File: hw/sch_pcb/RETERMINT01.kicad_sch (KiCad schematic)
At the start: 82 parts, among them J1 Conn_02x05_Odd_Even, J10 Raspberry_Pi_4, J11 RJ45_LED_Shielded, J2 Barrel_Jack_Switch, J3 HEADER_2x05_PARALLEL, J4 HEADER_2x01_PARALLEL, J5 HEADER_2x01_PARALLEL, J6 HEADER_2x01_PARALLEL, J7 HEADER_2x01_PARALLEL, J8 u.fl, J9 HEADER_2x01_PARALLEL, M1 HOLE, M2 HOLE, M3 HOLE, M4 HOLE, Q1 BC817-25, Q2 BC817-25, U1 TPSM33606S5QRDNRQ1, U2 USBLC6-2SC6, U3 MIC5504-3.3YM5, U4 NEO-M9N, U5 ADM2483xRW, U6 ADM2483xRW, U7 ADM2483xRW

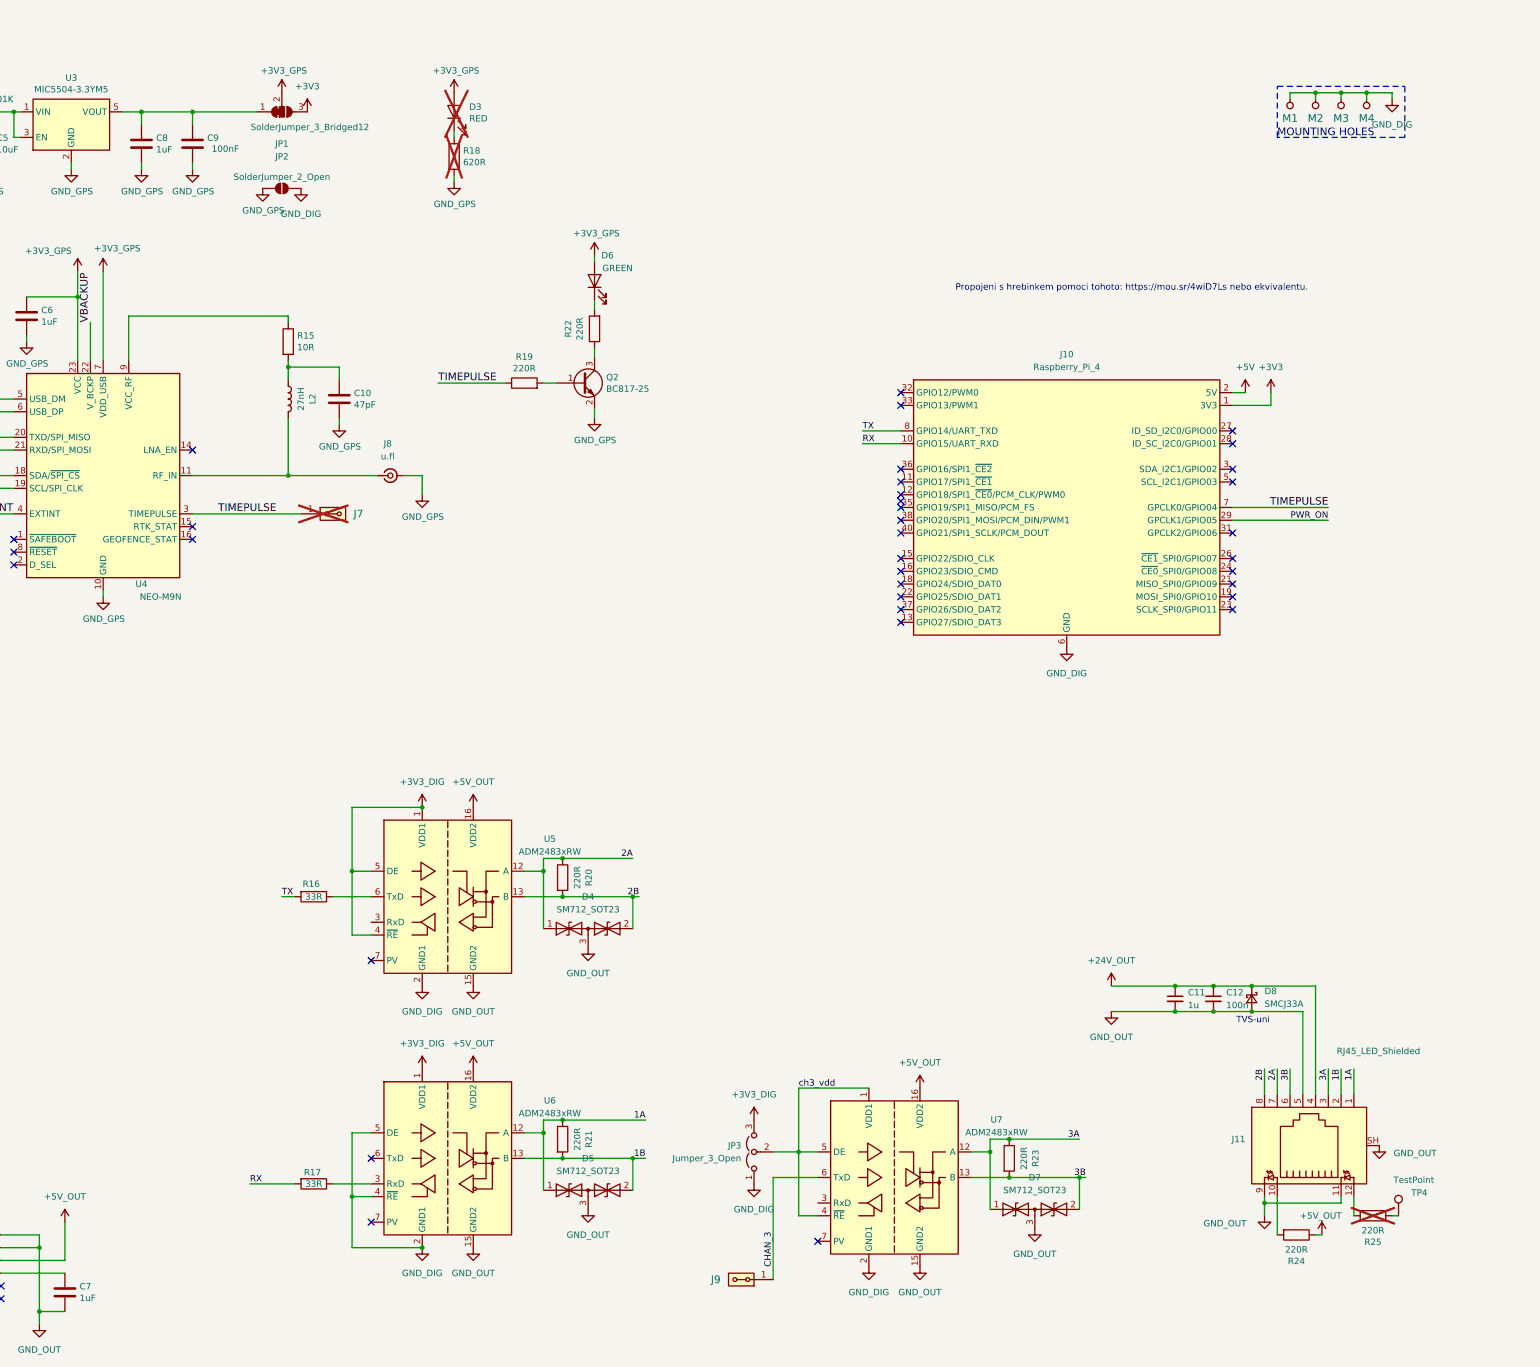
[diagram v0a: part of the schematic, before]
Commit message: Fix #2 Fix DRC errors. Improve layout.
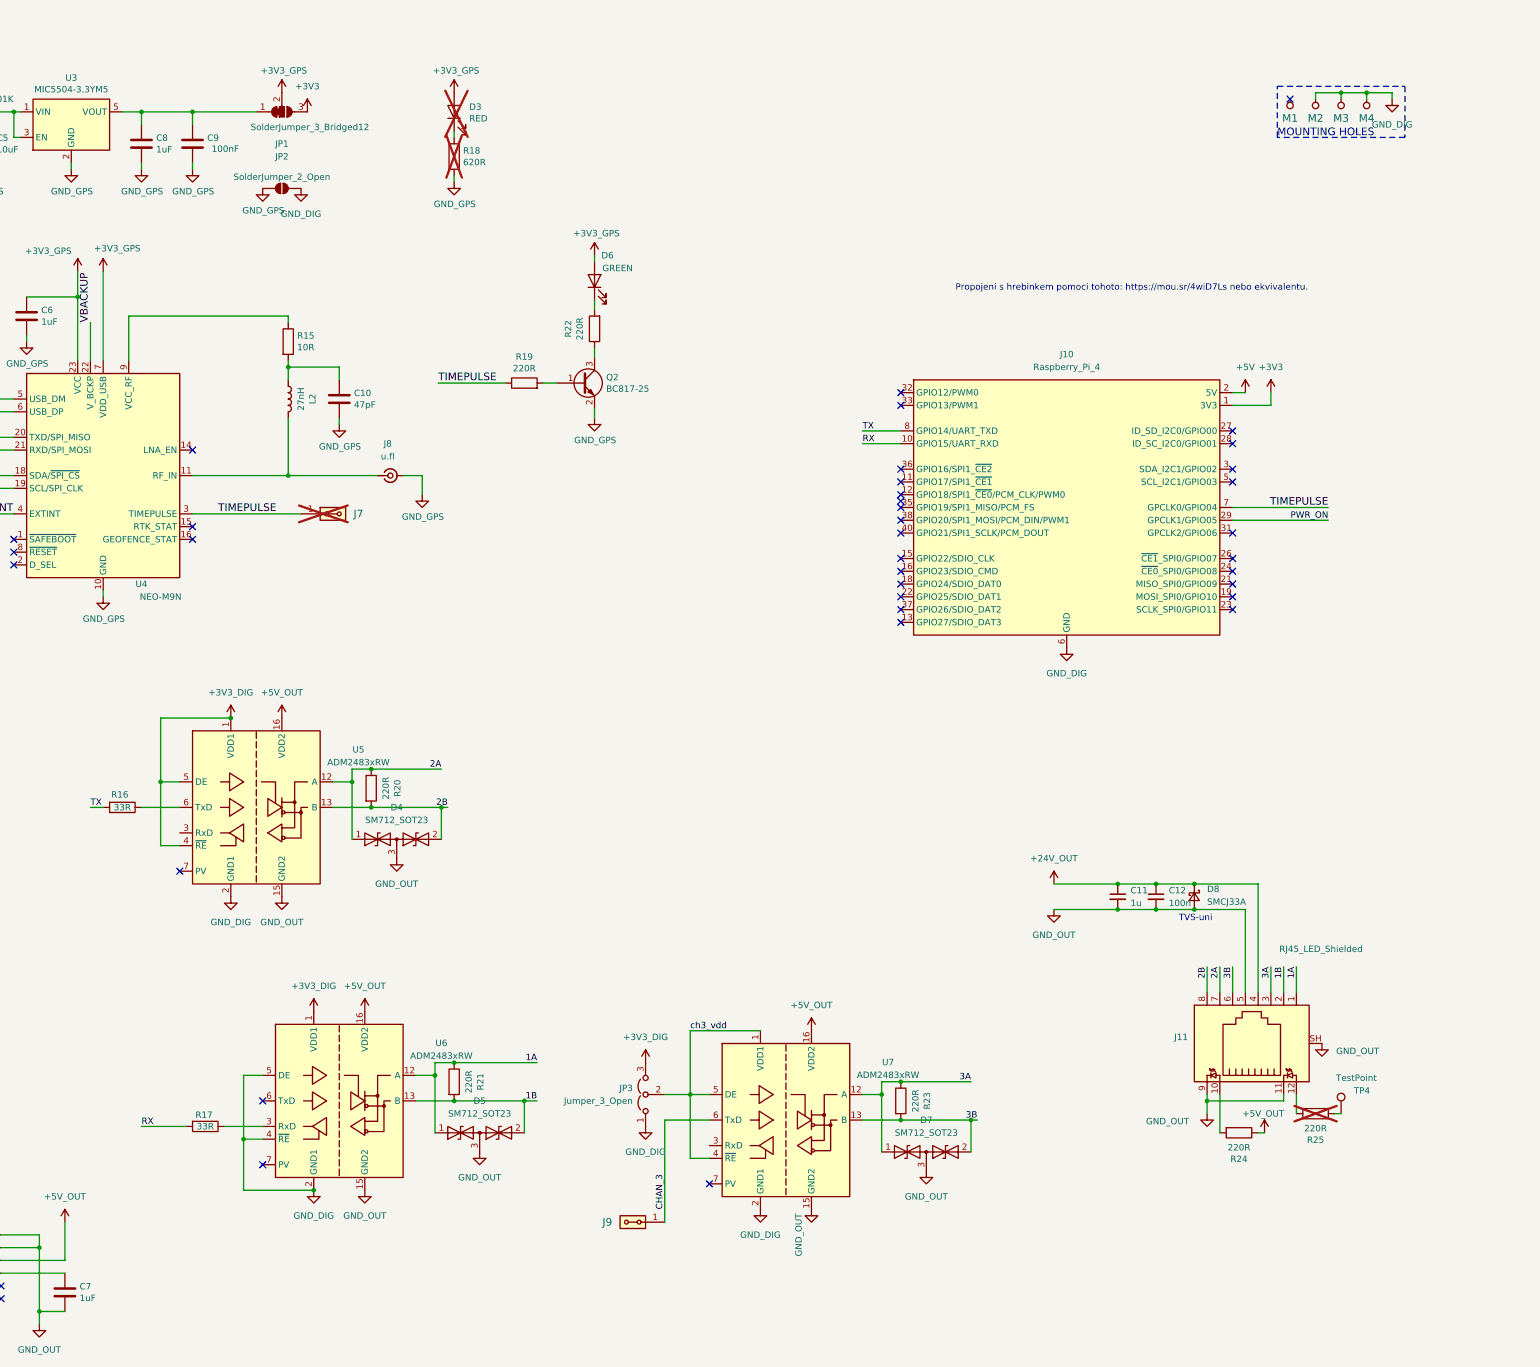
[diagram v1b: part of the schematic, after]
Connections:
- net GND_DIG: no longer M1.1
- no-connect marks 39 -> 40
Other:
- company: MLAB -> UST.cz
- title: RETERMINT01 – RETERMINAL DM Interface Board -> RETERMINT01A
- moved on the sheet: C11, C12, D4, D5, D7, D8, J11, J9, JP3, R16, R17, R20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

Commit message: Update component values.
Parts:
- C11, C2, C4: value 1u -> 1uF; UST_ID (none) -> 5c70984712875079b91f8b50
- C12, C3: value 100n -> 100nF; UST_ID (none) -> 5c70984712875079b91f8b4c
- D7: UST_ID (none) -> ?
- J8: UST_ID (none) -> 5ed7ac8e12875004e15a62c8
- R2: UST_ID (none) -> 5c70984512875079b91f898c
- R3, R4: UST_ID (none) -> 5c70984612875079b91f899f
- U4: UST_ID (none) -> 5fa0faaf12875025b3977985
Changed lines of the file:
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@@
 	(text "TVS-uni"
 		(exclude_from_sim no)
-		(at 358.394 184.658 0)
+		(at 359.41 185.42 0)
 		(effects
 			(font
@@
 			)
 		)
-		(property "UST_ID" ""
+		(property "UST_ID" "5fa0faaf12875025b3977985"
 			(at 140.97 96.52 0)
 			(hide yes)
@@
 			)
 		)
-		(property "Value" "1u"
+		(property "Value" "1uF"
 			(at 55.88 259.0862 0)
 			(show_name no)
@@
 			)
 		)
+		(property "UST_ID" "5c70984712875079b91f8b50"
+			(at 53.34 257.81 0)
+			(hide yes)
+			(show_name no)
+			(do_not_autoplace no)
+			(effects
+				(font
+					(size 1.27 1.27)
+				)
+			)
+		)
 		(pin "1"
 		)
@@
 		(in_pos_files yes)
 		(dnp no)
-		(fields_autoplaced yes)
 		(property "Reference" "C11"
-			(at 345.44 179.0762 0)
+			(at 340.36 175.26 0)
 			(show_name no)
 			(do_not_autoplace no)
@@
 			)
 		)
-		(property "Value" "1u"
-			(at 345.44 181.6162 0)
+		(property "Value" "1uF"
+			(at 336.55 180.34 0)
 			(show_name no)
 			(do_not_autoplace no)
@@
 			)
 		)
+		(property "UST_ID" "5c70984712875079b91f8b50"
+			(at 342.9 180.34 0)
+			(hide yes)
+			(show_name no)
+			(do_not_autoplace no)
+			(effects
+				(font
+					(size 1.27 1.27)
+				)
+			)
+		)
 		(pin "1"
 		)
@@
 		(in_pos_files yes)
 		(dnp no)
-		(fields_autoplaced yes)
 		(property "Reference" "D8"
-			(at 360.68 178.8159 90)
+			(at 356.87 175.26 90)
 			(show_name no)
 			(do_not_autoplace no)
@@
 		)
 		(property "Value" "SMCJ33A"
-			(at 360.68 181.3559 90)
+			(at 359.41 180.34 90)
 			(show_name no)
 			(do_not_autoplace no)
@@
 			)
 		)
-		(property "Value" "100n"
+		(property "Value" "100nF"
 			(at 43.18 259.0862 0)
 			(show_name no)
@@
 			)
 		)
+		(property "UST_ID" "5c70984712875079b91f8b4c"
+			(at 40.64 257.81 0)
+			(hide yes)
+			(show_name no)
+			(do_not_autoplace no)
+			(effects
+				(font
+					(size 1.27 1.27)
+				)
+			)
+		)
 		(pin "1"
 		)
@@
 		(in_pos_files yes)
 		(dnp no)
-		(fields_autoplaced yes)
 		(property "Reference" "D7"
-			(at 304.8 224.79 0)
+			(at 300.99 234.95 0)
 			(show_name no)
 			(do_not_autoplace no)
@@
 			)
 		)
+		(property "UST_ID" "?"
+			(at 304.8 231.14 0)
+			(hide yes)
+			(show_name no)
+			(do_not_autoplace no)
+			(effects
+				(font
+					(size 1.27 1.27)
+				)
+			)
+		)
 		(pin "1"
 		)
@@
 			)
 		)
-		(property "UST_ID" ""
+		(property "UST_ID" "5c70984612875079b91f899f"
 			(at 36.83 215.9 0)
 			(hide yes)
@@
 		(in_pos_files yes)
 		(dnp no)
-		(fields_autoplaced yes)
 		(property "Reference" "D4"
-			(at 199.39 162.56 0)
+			(at 203.2 172.72 0)
 			(show_name no)
 			(do_not_autoplace no)
@@
 			)
 		)
-		(property "UST_ID" ""
+		(property "UST_ID" "5c70984612875079b91f899f"
 			(at 36.83 208.28 0)
 			(hide yes)
@@
 		(in_pos_files yes)
 		(dnp no)
-		(fields_autoplaced yes)
 		(property "Reference" "D5"
-			(at 215.9 220.98 0)
+			(at 220.98 231.14 0)
 			(show_name no)
 			(do_not_autoplace no)
@@
 			)
 		)
+		(property "UST_ID" "5ed7ac8e12875004e15a62c8"
+			(at 198.12 96.52 0)
+			(hide yes)
+			(show_name no)
+			(do_not_autoplace no)
+			(effects
+				(font
+					(size 1.27 1.27)
+				)
+			)
+		)
 		(pin "2"
 		)
@@
 			)
 		)
-		(property "UST_ID" ""
+		(property "UST_ID" "5c70984512875079b91f898c"
 			(at 31.75 212.09 0)
 			(hide yes)
@@
 		(in_pos_files yes)
 		(dnp no)
-		(fields_autoplaced yes)
 		(property "Reference" "C12"
-			(at 353.06 179.0762 0)
+			(at 347.98 175.26 0)
 			(show_name no)
 			(do_not_autoplace no)
@@
 			)
 		)
-		(property "Value" "100n"
-			(at 353.06 181.6162 0)
+		(property "Value" "100nF"
+			(at 346.71 185.42 0)
 			(show_name no)
 			(do_not_autoplace no)
@@
 			)
 		)
+		(property "UST_ID" "5c70984712875079b91f8b4c"
+			(at 350.52 180.34 0)
+			(hide yes)
+			(show_name no)
+			(do_not_autoplace no)
+			(effects
+				(font
+					(size 1.27 1.27)
+				)
+			)
+		)
 		(pin "1"
 		)
@@
 			)
 		)
-		(property "Value" "1u"
+		(property "Value" "1uF"
 			(at 31.75 259.0862 0)
 			(show_name no)
@@
 			)
 		)
+		(property "UST_ID" "5c70984712875079b91f8b50"
+			(at 29.21 257.81 0)
+			(hide yes)
+			(show_name no)
+			(do_not_autoplace no)
+			(effects
+				(font
+					(size 1.27 1.27)
+				)
+			)
+		)
 		(pin "1"
 		)
@@
 		(in_pos_files yes)
 		(dnp no)
-		(fields_autoplaced yes)
 		(property "Reference" "U7"
-			(at 297.18 213.2898 0)
+			(at 276.86 207.01 0)
 			(show_name no)
 			(do_not_autoplace no)
@@
 		)
 		(property "Value" "ADM2483xRW"
-			(at 297.18 215.8298 0)
+			(at 290.83 207.01 0)
 			(show_name no)
 			(do_not_autoplace no)

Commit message: fix issues
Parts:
- added C13, C14, C15, C16, C17, C18: 100nF, Capacitor_SMD:C_0805_2012Metric, symbol Device:C_Small
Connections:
- net +3V3_DIG is gone; now on net +3V3: JP3.3 (B), U5.1 (VDD1), U5.4 (~{RE}), U5.5 (DE), U6.1 (VDD1)
- net +3V3: now also U7.1 (VDD1), C13.1, C15.1, C17.1
- net +5V_OUT: now also C14.1, C16.1, C18.1
- net GND_DIG: now also C13.2, C15.2, C17.2
- net GND_OUT: now also C14.2, C16.2, C18.2
- net PWR_ON: now also J10.22 (GPIO25/SDIO_DAT1); no longer J10.29 (GPCLK1/GPIO05)
- net TIMEPULSE: now also J10.18 (GPIO24/SDIO_DAT0); no longer J10.7 (GPCLK0/GPIO04)
- net ch3_vdd: no longer names the net of JP3.2 (C), U7.4 (~{RE}), U7.5 (DE)
- net ch3_vdd: no longer U7.1 (VDD1)
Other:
- title: RETERMINT01A -> RETERMINT01B
